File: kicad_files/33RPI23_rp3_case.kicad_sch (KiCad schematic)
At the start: 106 parts, among them CN1 HDMI, J1 VGA, J10 AudioJack4, J11 USB_B_Micro, J12 Mini-DIN-6, J13 Mini-DIN-6, J14 Conn_01x07, J15 Conn_01x01_Female, J16 USB, J17 Conn_01x02_Female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

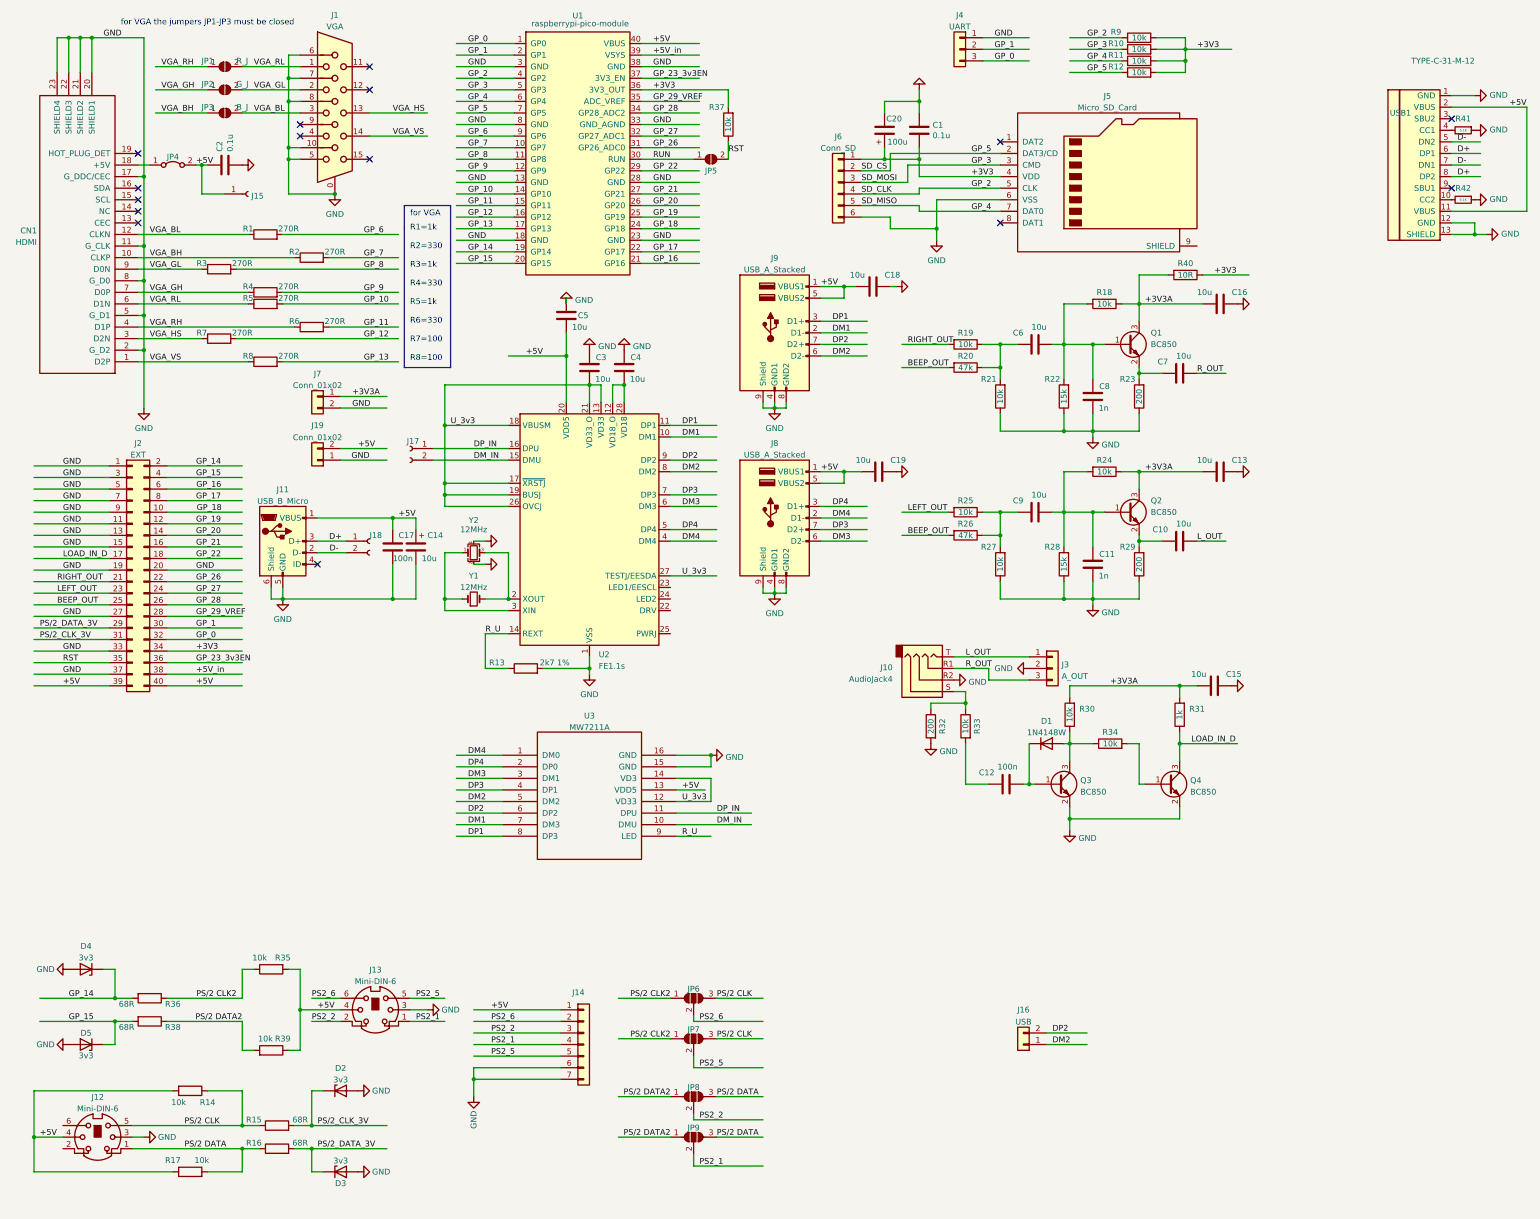
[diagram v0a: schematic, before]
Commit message: .
Power Led
USB IN d+ d- position
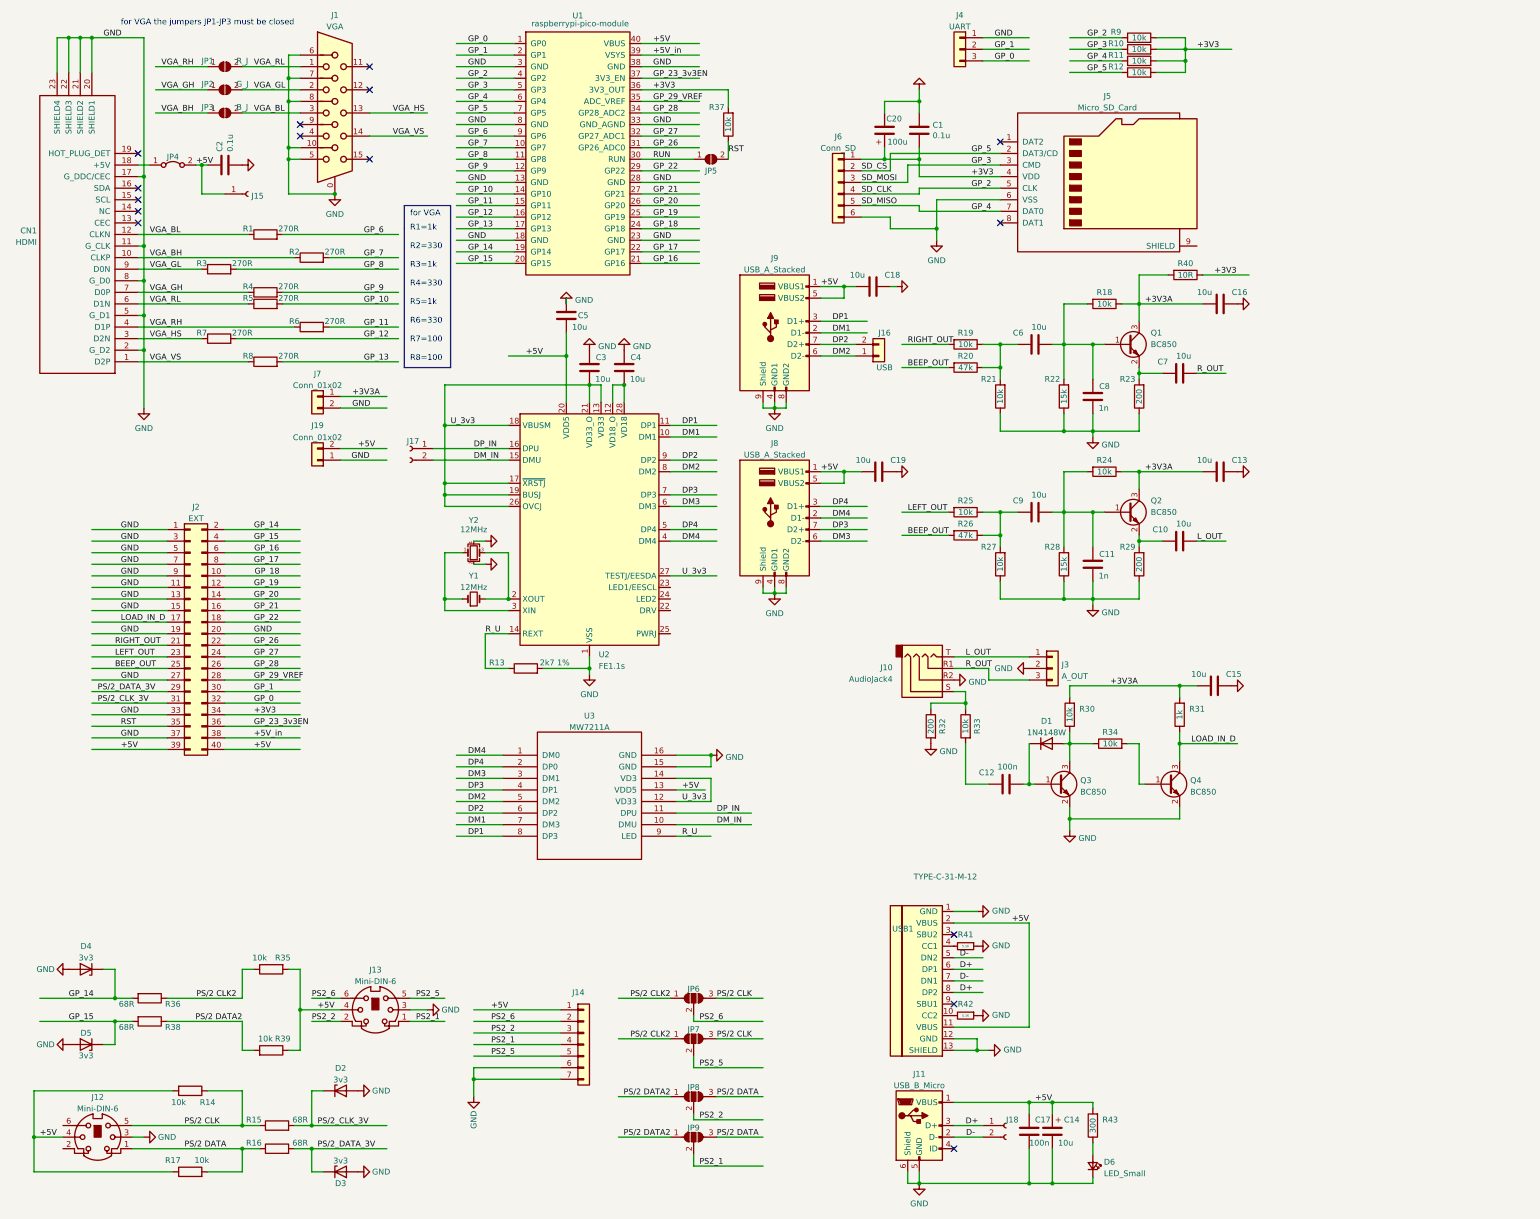
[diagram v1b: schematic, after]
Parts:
- added D6: LED_Small, LED_SMD:LED_1206_3216Metric_Pad1.42x1.75mm_HandSolder, symbol Device:LED_Small
- added R43: 300, Resistor_SMD:R_0805_2012Metric_Pad1.20x1.40mm_HandSolder, symbol Device:R
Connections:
- net +5V: now also R43.2
- net GND: now also D6.1 (K)
- new net: D6.2 (A), R43.1
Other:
- moved on the sheet: C14, C17, J11, J16, J18, J2, R41, R42, USB1

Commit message: labels
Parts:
- added J20: Conn_01x02, Connector_PinHeader_2.54mm:PinHeader_1x02_P2.54mm_Vertical, symbol Connector_Generic:Conn_01x02
- added R44: 10k, Resistor_SMD:R_0805_2012Metric_Pad1.20x1.40mm_HandSolder, symbol Device:R
- C14: value 10u -> 100u
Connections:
- net GND: now also J20.1 (Pin_1)
- net at C12.1, R33.2: now also R44.2
- new net: J20.2 (Pin_2), R44.1
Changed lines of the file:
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@@
   (junction (at 222.25 165.1) (diameter 0) (color 0 0 0 0)
   )
+  (junction (at 222.25 182.88) (diameter 0) (color 0 0 0 0)
+  )
   (junction (at 243.84 142.24) (diameter 0) (color 0 0 0 0)
   )
@@
     (stroke (width 0) (type default) (color 0 0 0 0))
   )
+  (wire (pts (xy 208.28 182.88) (xy 212.09 182.88))
+    (stroke (width 0) (type default) (color 0 0 0 0))
+  )
   (wire (pts (xy 59.69 134.62) (xy 76.2 134.62))
     (stroke (width 0) (type default) (color 0 0 0 0))
@@
     (stroke (width 0) (type default) (color 0 0 0 0))
   )
+  (wire (pts (xy 209.55 185.42) (xy 209.55 193.04))
+    (stroke (width 0) (type default) (color 0 0 0 0))
+  )
   (wire (pts (xy 17.78 260.35) (xy 24.13 260.35))
     (stroke (width 0) (type default) (color 0 0 0 0))
@@
     (stroke (width 0) (type default) (color 0 0 0 0))
   )
+  (wire (pts (xy 219.71 182.88) (xy 222.25 182.88))
+    (stroke (width 0) (type default) (color 0 0 0 0))
+  )
   (wire (pts (xy 59.69 152.4) (xy 76.2 152.4))
     (stroke (width 0) (type default) (color 0 0 0 0))
@@
     (stroke (width 0) (type default) (color 0 0 0 0))
   )
+  (wire (pts (xy 208.28 185.42) (xy 209.55 185.42))
+    (stroke (width 0) (type default) (color 0 0 0 0))
+  )
   (wire (pts (xy 107.95 119.38) (xy 107.95 121.92))
     (stroke (width 0) (type default) (color 0 0 0 0))
@@
     (pin "2")
   )
+  (symbol (lib_id "Device:R") (at 215.9 182.88 90) (mirror x) (unit 1)
+    (in_bom yes) (on_board yes)
+    (property "Reference" "R44" (id 0) (at 215.9 180.34 90))
+    (property "Value" "10k" (id 1) (at 215.9 182.88 90))
+    (property "Footprint" "Resistor_SMD:R_0805_2012Metric_Pad1.20x1.40mm_HandSolder" (id 2) (at 215.9 181.102 90)
+      (effects (font (size 1.27 1.27)) hide)
+    )
+    (property "Datasheet" "~" (id 3) (at 215.9 182.88 0)
+      (effects (font (size 1.27 1.27)) hide)
+    )
+    (pin "1")
+    (pin "2")
+  )
   (symbol (lib_id "Device:R") (at 252.73 77.47 270) (unit 1)
     (in_bom yes) (on_board yes)
@@
       (effects (font (size 1.27 1.27)) (justify left))
     )
-    (property "Value" "10u" (id 1) (at 242.57 261.62 0)
+    (property "Value" "100u" (id 1) (at 242.57 261.62 0)
       (effects (font (size 1.27 1.27)) (justify left))
     )
@@
     (pin "1")
   )
+  (symbol (lib_id "Connector_Generic:Conn_01x02") (at 203.2 185.42 180) (unit 1)
+    (in_bom yes) (on_board yes)
+    (property "Reference" "J20" (id 0) (at 203.2 177.8 0))
+    (property "Value" "Conn_01x02" (id 1) (at 203.2 180.4471 0))
+    (property "Footprint" "Connector_PinHeader_2.54mm:PinHeader_1x02_P2.54mm_Vertical" (id 2) (at 203.2 185.42 0)
+      (effects (font (size 1.27 1.27)) hide)
+    )
+    (property "Datasheet" "~" (id 3) (at 203.2 185.42 0)
+      (effects (font (size 1.27 1.27)) hide)
+    )
+    (pin "1")
+    (pin "2")
+  )
   (symbol (lib_id "Jumper:SolderJumper_2_Open") (at 59.69 30.48 0) (unit 1)
     (in_bom yes) (on_board yes)
@@
     (pin "2")
   )
+  (symbol (lib_id "power:GND") (at 209.55 193.04 0) (unit 1)
+    (in_bom yes) (on_board yes) (fields_autoplaced)
+    (property "Reference" "#PWR0124" (id 0) (at 209.55 199.39 0)
+      (effects (font (size 1.27 1.27)) hide)
+    )
+    (property "Value" "GND" (id 1) (at 211.455 194.7438 0)
+      (effects (font (size 1.27 1.27)) (justify left))
+    )
+    (property "Footprint" "" (id 2) (at 209.55 193.04 0)
+      (effects (font (size 1.27 1.27)) hide)
+    )
+    (property "Datasheet" "" (id 3) (at 209.55 193.04 0)
+      (effects (font (size 1.27 1.27)) hide)
+    )
+    (pin "1")
+  )
   (symbol (lib_id "Jumper:SolderJumper_2_Open") (at 59.69 35.56 0) (unit 1)
     (in_bom yes) (on_board yes)
@@
       (reference "#PWR0123") (unit 1) (value "GND") (footprint "")
     )
+    (path "/ec84282d-1b30-4a9b-b323-7fb18c9d30bc"
+      (reference "#PWR0124") (unit 1) (value "GND") (footprint "")
+    )
     (path "/474d8346-b157-4d0c-8582-d2573a7438f0"
       (reference "C1") (unit 1) (value "0.1u") (footprint "Capacitor_SMD:C_0805_2012Metric_Pad1.18x1.45mm_HandSolder")
@@
     )
     (path "/0ba96109-2f5f-4937-9876-45c6c789189a"
-      (reference "C14") (unit 1) (value "10u") (footprint "LIBS:c_comb_pol")
+      (reference "C14") (unit 1) (value "100u") (footprint "LIBS:c_comb_pol")
     )
     (path "/17a071f0-f8db-42f6-9c95-abad7a024749"
@@
       (reference "J19") (unit 1) (value "Conn_01x02") (footprint "Connector_PinHeader_2.54mm:PinHeader_1x02_P2.54mm_Vertical")
     )
+    (path "/c2c6a19c-5a63-491a-b9c3-b3435c46b4ff"
+      (reference "J20") (unit 1) (value "Conn_01x02") (footprint "Connector_PinHeader_2.54mm:PinHeader_1x02_P2.54mm_Vertical")
+    )
     (path "/7813d41d-0fb2-4ae2-9cd2-80bee7140c73"
       (reference "JP1") (unit 1) (value "R_J") (footprint "Jumper:SolderJumper-2_P1.3mm_Open_RoundedPad1.0x1.5mm")
@@
       (reference "R43") (unit 1) (value "300") (footprint "Resistor_SMD:R_0805_2012Metric_Pad1.20x1.40mm_HandSolder")
     )
+    (path "/05ce9507-ce94-49f4-bf97-083fd6932ab4"
+      (reference "R44") (unit 1) (value "10k") (footprint "Resistor_SMD:R_0805_2012Metric_Pad1.20x1.40mm_HandSolder")
+    )
     (path "/46d595f4-edb0-4ded-805c-1668608db359"
